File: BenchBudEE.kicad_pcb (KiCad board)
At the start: 2 copper layers, 0 parts

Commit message: Basic PCB setup done and changed some preferences
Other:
- board outline added: 165.1 x 63.5 mm
- copper layers 2 -> 4
- rule trace_min: 0.254 -> 0.1524
- rule via_min_drill: 0.508 -> 0.3302
- rule via_min_size: 0.889 -> 0.508
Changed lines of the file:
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@@
     (area 0 0 0 0)
     (thickness 1.6)
-    (drawings 0)
+    (drawings 4)
     (tracks 0)
     (zones 0)
@@
     (nets 1)
   )
-  (page A4)
+  (page A3)
+  (title_block
+    (title BenchBudEE)
+    (company ee-lco)
+  )
   (layers
     (15 F.Cu signal)
+    (2 PWR power)
+    (1 GND power)
     (0 B.Cu signal)
     (16 B.Adhes user)
@@
     (22 B.Mask user)
     (23 F.Mask user)
-    (24 Dwgs.User user)
-    (25 Cmts.User user)
-    (26 Eco1.User user)
-    (27 Eco2.User user)
     (28 Edge.Cuts user)
   )
   (setup
     (last_trace_width 0.254)
+    (user_trace_width 0.1524)
     (trace_clearance 0.254)
     (zone_clearance 0.508)
     (zone_45_only no)
-    (trace_min 0.254)
+    (trace_min 0.1524)
     (segment_width 0.2)
     (edge_width 0.1)
     (via_size 0.889)
     (via_drill 0.635)
-    (via_min_size 0.889)
-    (via_min_drill 0.508)
+    (via_min_size 0.508)
+    (via_min_drill 0.3302)
+    (user_via 0.508 0.3302)
     (uvia_size 0.508)
     (uvia_drill 0.127)
@@
     (pad_to_mask_clearance 0)
     (aux_axis_origin 0 0)
-    (visible_elements FFFFF77F)
+    (visible_elements FFFFFF7F)
     (pcbplotparams
       (layerselection 3178497)
@@
     (add_net "")
   )
+  (gr_line (start 129.54 111.76) (end 129.54 175.26) (angle 90) (layer Edge.Cuts) (width 0.1))
+  (gr_line (start 294.64 111.76) (end 129.54 111.76) (angle 90) (layer Edge.Cuts) (width 0.1))
+  (gr_line (start 294.64 175.26) (end 294.64 111.76) (angle 90) (layer Edge.Cuts) (width 0.1))
+  (gr_line (start 129.54 175.26) (end 294.64 175.26) (angle 90) (layer Edge.Cuts) (width 0.1))
 )

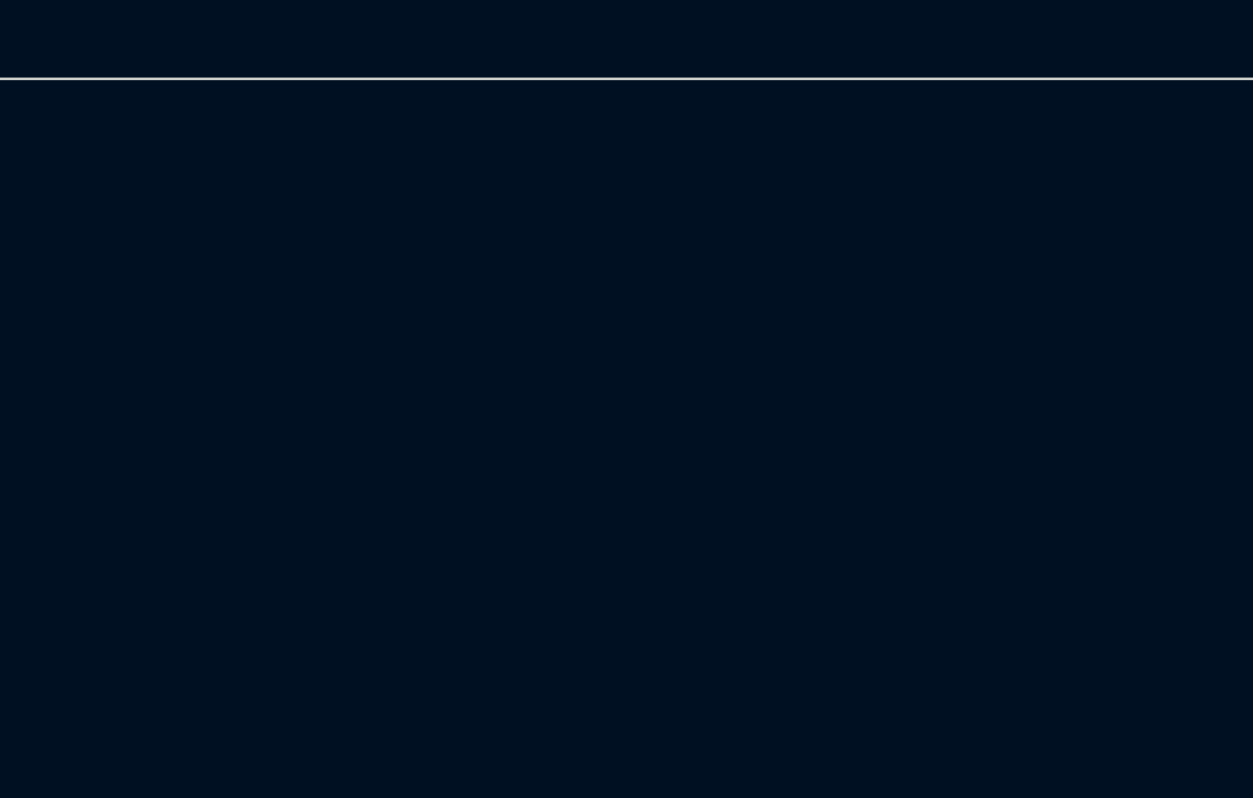
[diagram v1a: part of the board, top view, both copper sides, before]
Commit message: Added footprints for the relay module, preliminarily annotated schematic, relay components placed on PCB
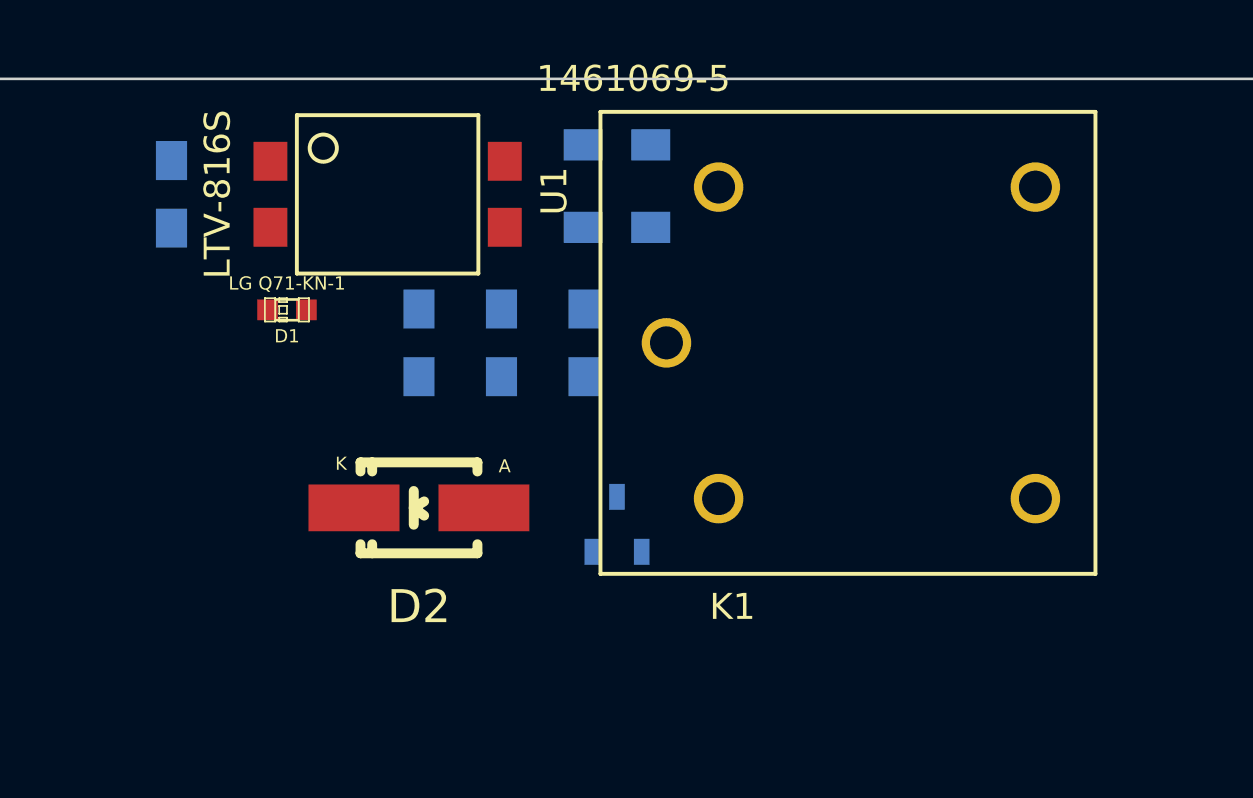
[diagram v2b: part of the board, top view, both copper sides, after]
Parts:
- added D1: LG Q71-KN-1, LEDs:LED-0603, F.Cu at (245.7, 120.7)
- added D2: B130-13-F, Diodes_SMD:Diode-SMA_Handsoldering, F.Cu at (250.8, 128.3)
- added K1: 1461069-5, BenchBudEE:TE-SPDT, F.Cu at (260.4, 121.9)
- added Q1: 2N3404, Transistors_SMD:sot23, B.Cu at (258.4, 128.9)
- added R1: 500, Resistors_SMD:Resistor_SMD0805_HandSoldering, B.Cu at (241.3, 116.2)
- added R2: 200, Resistors_SMD:Resistor_SMD0805_HandSoldering, B.Cu at (250.8, 121.9)
- added R3: 100, Resistors_SMD:Resistor_SMD0805_HandSoldering, B.Cu at (257.2, 121.9)
- added R4: 0, Resistors_SMD:Resistor_SMD0805_HandSoldering, B.Cu at (258.4, 114.3)
- added R5: 0, Resistors_SMD:Resistor_SMD0805_HandSoldering, B.Cu at (258.4, 117.5)
- added R6: 0, Resistors_SMD:Resistor_SMD0805_HandSoldering, B.Cu at (254.0, 121.9)
- added U1: LTV-816S, BenchBudEE:4-SMD, F.Cu at (245.1, 114.9)

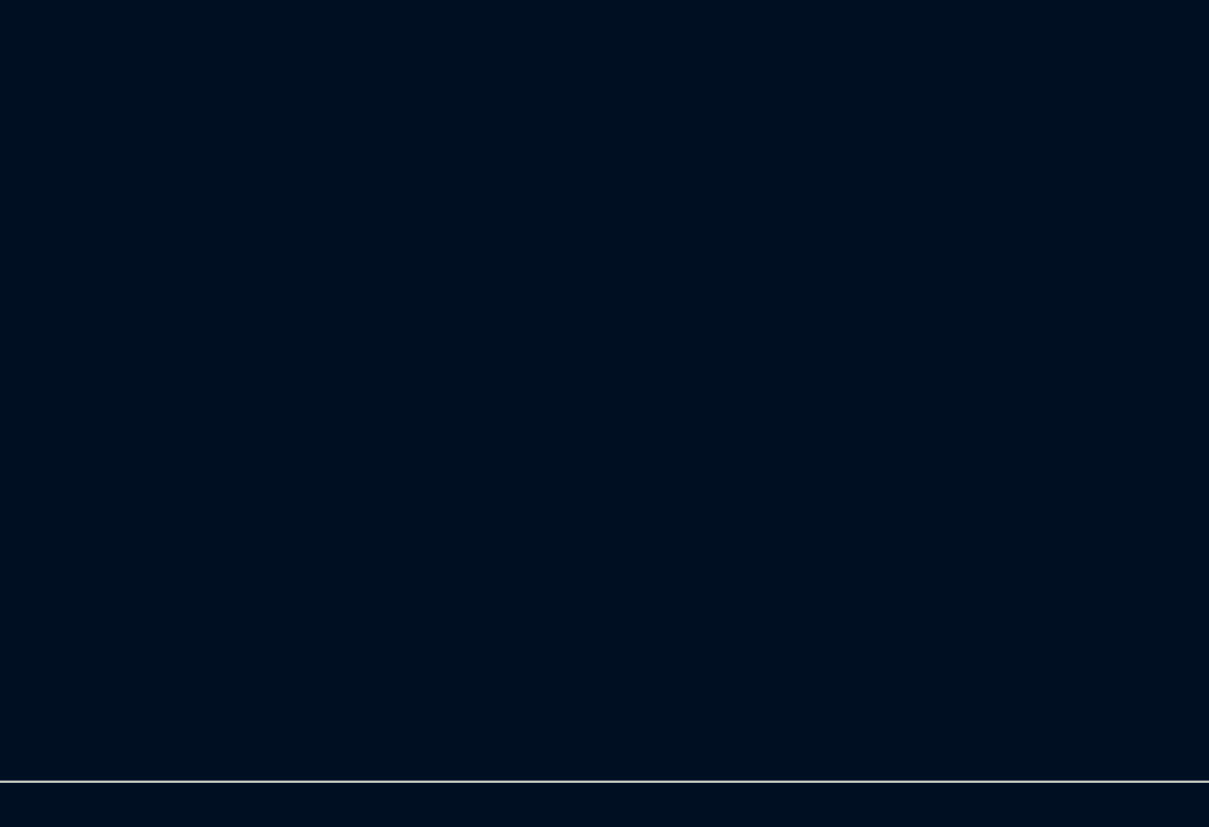
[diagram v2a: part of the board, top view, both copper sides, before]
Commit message: Associated and placed the thermocouple module
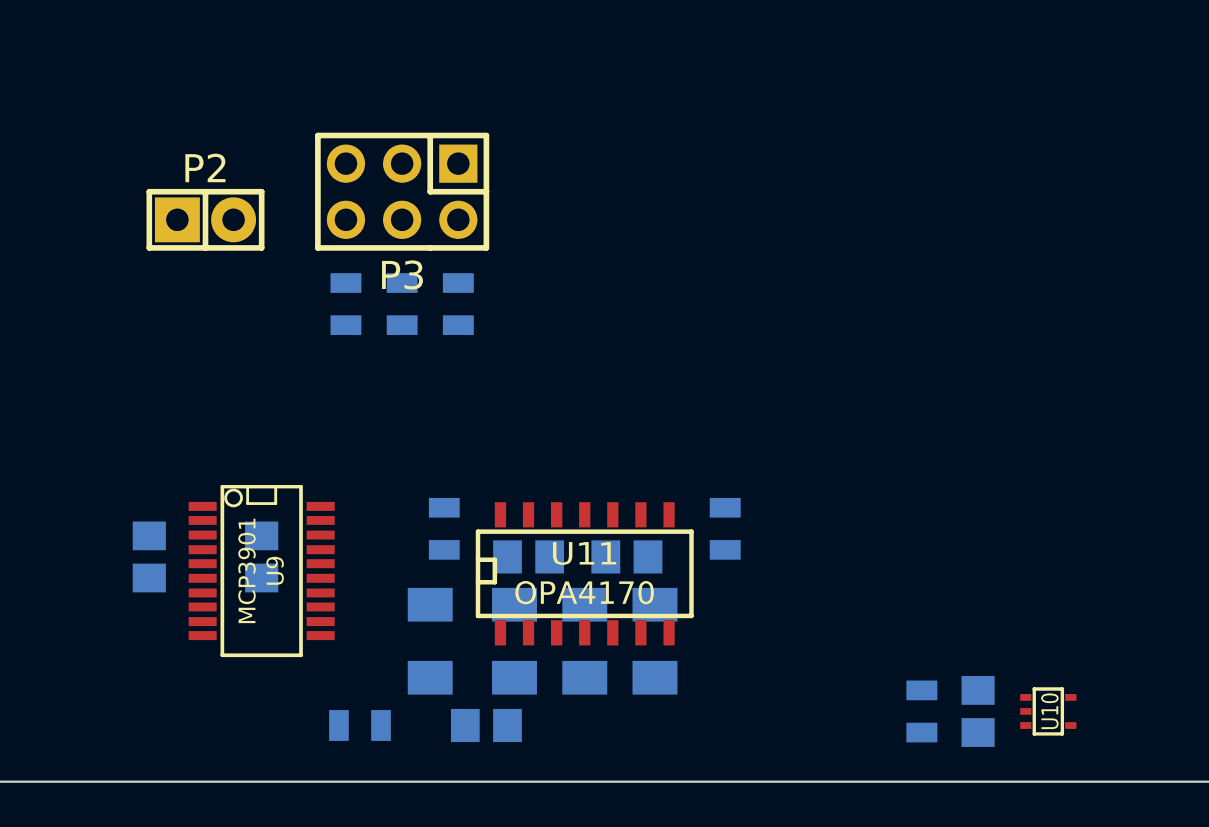
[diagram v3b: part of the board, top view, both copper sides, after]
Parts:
- added C10: C, Capacitors_SMD:c_0805, B.Cu at (255.9, 172.1)
- added C5: C, Capacitors_SMD:c_0805, B.Cu at (223.5, 165.1)
- added C6: C, Capacitors_SMD:c_0805, B.Cu at (218.4, 165.1)
- added C7: C, Capacitors_SMD:c_0805, B.Cu at (233.7, 172.7)
- added C8: C, Capacitors_SMD:c_0805, B.Cu at (235.6, 165.1)
- added C9: C, Capacitors_SMD:c_0805, B.Cu at (240.0, 165.1)
- added P2: CONN_2, Pin_Headers:Pin_Header_Straight_1x02, F.Cu at (221.0, 149.9)
- added P3: CONN_3X2, Pin_Headers:Pin_Header_Straight_2x03, F.Cu at (229.9, 148.6)
- added R21: R, SMD_Packages:SM1206, B.Cu at (238.1, 168.9)
- added R22: R, SMD_Packages:SM1206, B.Cu at (231.1, 168.9)
- added R23: R, SMD_Packages:SM1206, B.Cu at (241.3, 168.9)
- added R24: R, SMD_Packages:SM1206, B.Cu at (234.9, 168.9)
- added R25: R, SMD_Packages:SM0805, B.Cu at (244.5, 163.8)
- added R26: R, SMD_Packages:SM0805, B.Cu at (227.3, 153.7)
- added R27: R, SMD_Packages:SM0805, B.Cu at (231.8, 163.8)
- added R43: R, SMD_Packages:SM0805, B.Cu at (229.9, 153.7)
- added R44: R, SMD_Packages:SM0805, B.Cu at (232.4, 153.7)
- added R47: R, SMD_Packages:SM0805, B.Cu at (253.4, 172.1)
- added R48: R, SMD_Packages:SM0805, B.Cu at (228.0, 172.7)
- added U10: LMT84, SMD_Packages:SOT353, F.Cu at (259.1, 172.1)
- added U11: OPA4170, SMD_Packages:SO14E, F.Cu at (238.1, 165.7)
- added U9: MCP3901, SMD_Packages:SSOP20, F.Cu at (223.5, 165.7)

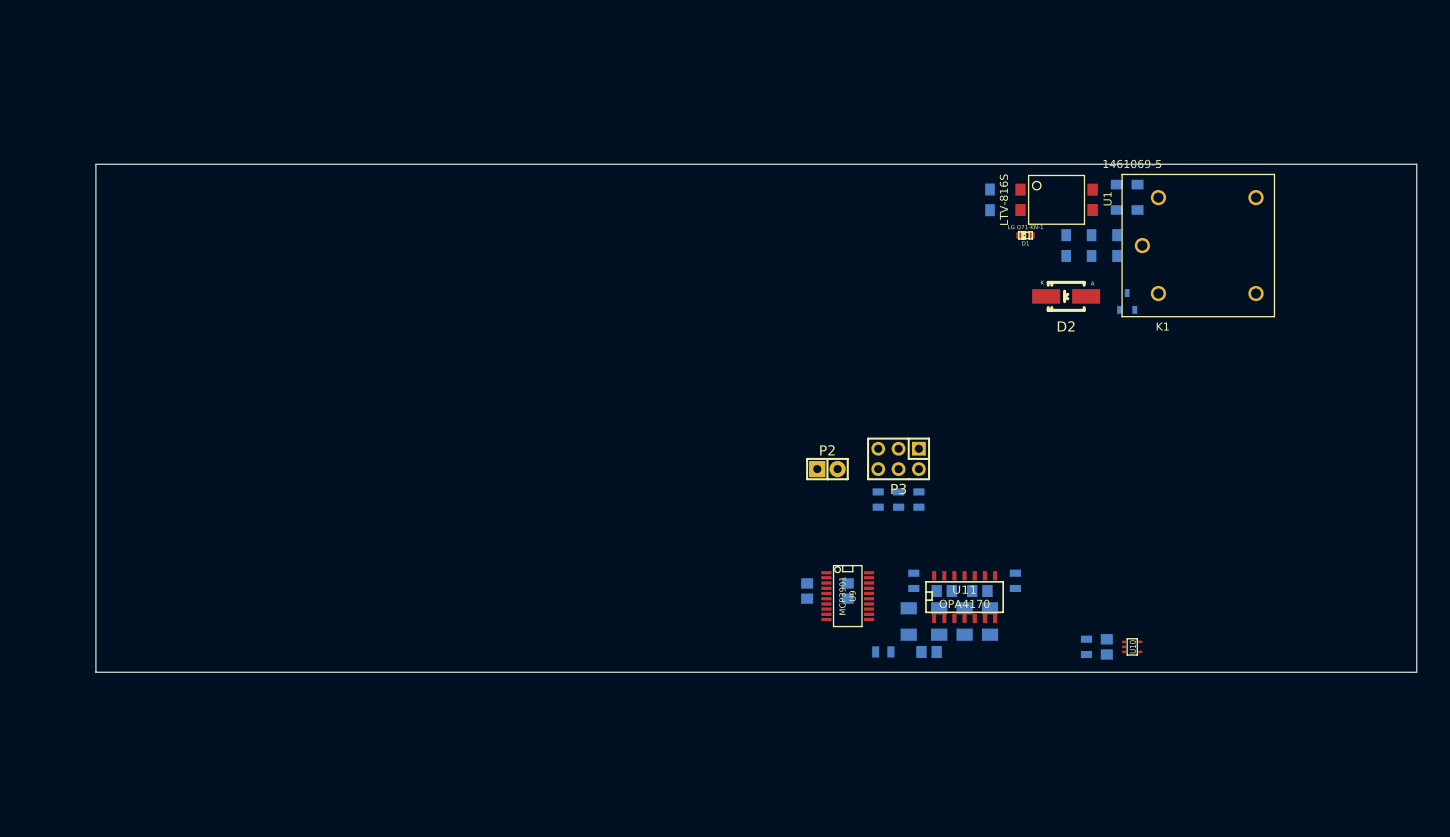
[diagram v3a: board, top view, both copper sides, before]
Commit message: Associated and placed the terminal blocks and ATX header
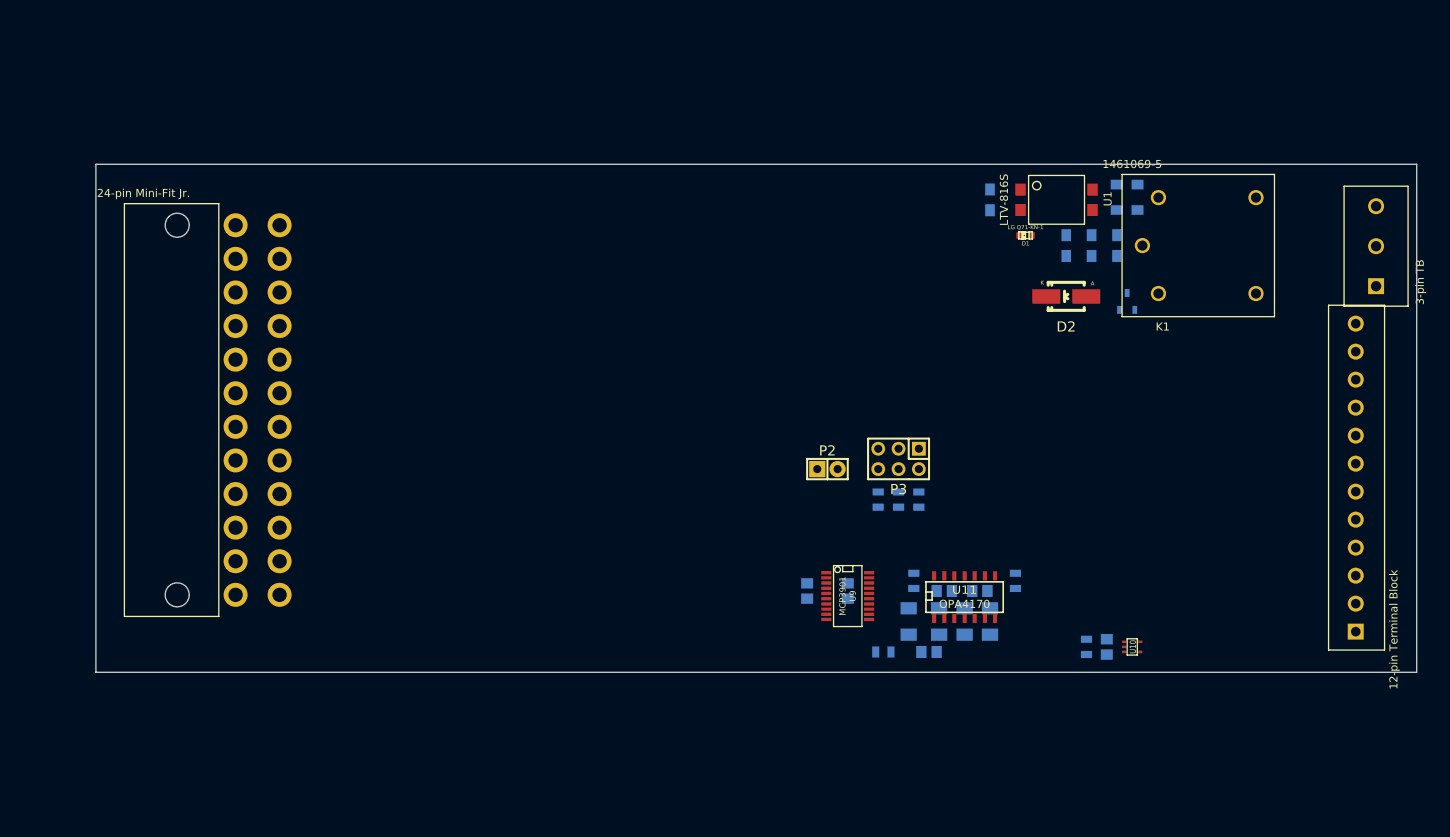
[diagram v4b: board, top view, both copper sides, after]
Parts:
- added P1: 24-pin Mini-Fit Jr., BenchBudEE:ATX_Header, F.Cu at (139.7, 119.4)
- added P4: 12-pin Terminal Block, BenchBudEE:12pinTB, F.Cu at (287.0, 170.2)
- added P5: 3-pin TB, BenchBudEE:3pinTB, F.Cu at (289.6, 127.0)

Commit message: Associated and placed the Arduino
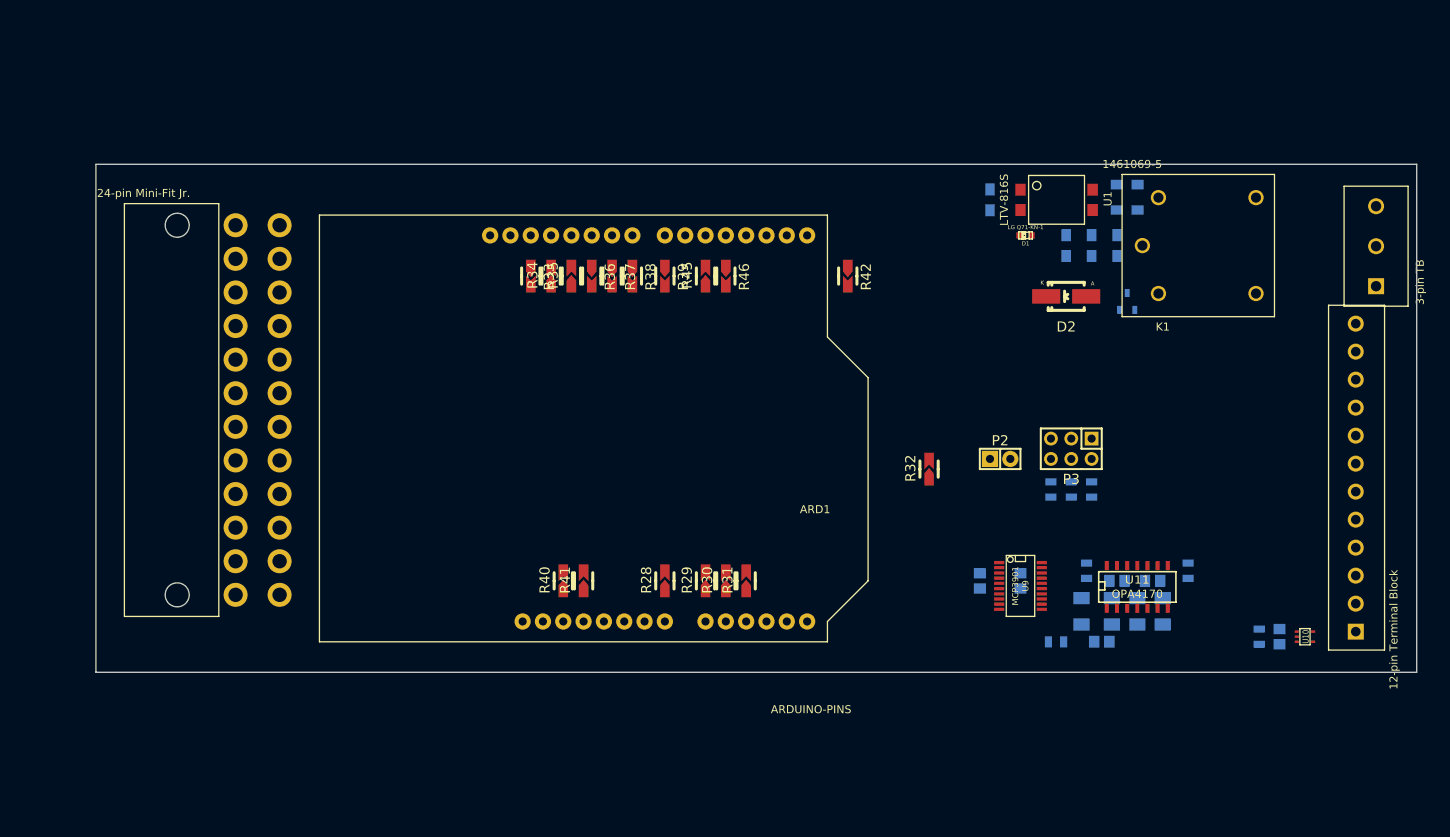
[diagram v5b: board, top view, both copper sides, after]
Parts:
- added ARD1: ARDUINO-PINS, BenchBudEE:Arduino, F.Cu at (218.4, 168.9)
- added R28: R, BenchBudEE:Resistor_SMD0805_Blob, F.Cu at (200.7, 163.8)
- added R29: R, BenchBudEE:Resistor_SMD0805_Blob, F.Cu at (205.7, 163.8)
- added R30: R, BenchBudEE:Resistor_SMD0805_Blob, F.Cu at (208.3, 163.8)
- added R31: R, BenchBudEE:Resistor_SMD0805_Blob, F.Cu at (210.8, 163.8)
- added R32: R, BenchBudEE:Resistor_SMD0805_Blob, F.Cu at (233.7, 149.9)
- added R33: R, BenchBudEE:Resistor_SMD0805_Blob, F.Cu at (183.9, 125.7)
- added R34: R, BenchBudEE:Resistor_SMD0805_Blob, F.Cu at (186.4, 125.7)
- added R35: R, BenchBudEE:Resistor_SMD0805_Blob, F.Cu at (189.0, 125.7)
- added R36: R, BenchBudEE:Resistor_SMD0805_Blob, F.Cu at (191.5, 125.7)
- added R37: R, BenchBudEE:Resistor_SMD0805_Blob, F.Cu at (194.1, 125.7)
- added R38: R, BenchBudEE:Resistor_SMD0805_Blob, F.Cu at (196.6, 125.7)
- added R39: R, BenchBudEE:Resistor_SMD0805_Blob, F.Cu at (200.7, 125.7)
- added R40: R, BenchBudEE:Resistor_SMD0805_Blob, F.Cu at (188.0, 163.8)
- added R41: R, BenchBudEE:Resistor_SMD0805_Blob, F.Cu at (190.5, 163.8)
- added R42: R, BenchBudEE:Resistor_SMD0805_Blob, F.Cu at (223.5, 125.7)
- added R45: R, BenchBudEE:Resistor_SMD0805_Blob, F.Cu at (205.7, 125.7)
- added R46: R, BenchBudEE:Resistor_SMD0805_Blob, F.Cu at (208.3, 125.7)
- moved R24 21.6 mm to (256.5, 167.6)
- moved U10 21.6 mm to (280.7, 170.8)
- moved C10 21.6 mm to (277.5, 170.8)
- moved C7 21.6 mm to (255.3, 171.4)
- moved P2 21.6 mm to (242.6, 148.6)
- moved P3 21.6 mm to (251.5, 147.3)
- moved R22 21.6 mm to (252.7, 167.6)
- moved R25 21.6 mm to (266.1, 162.6)
- moved R27 21.6 mm to (253.4, 162.6)
- moved R48 21.6 mm to (249.6, 171.4)
- moved U9 21.6 mm to (245.1, 164.5)
- moved C5 21.6 mm to (245.1, 163.8)
- moved C6 21.6 mm to (240.0, 163.8)
- moved C8 21.6 mm to (257.2, 163.8)
- moved C9 21.6 mm to (261.6, 163.8)
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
